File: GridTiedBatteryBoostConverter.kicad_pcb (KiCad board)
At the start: 2 copper layers, 270.1 x 143.1 mm, 160 parts, among them J101 Battery Connection, J103 Solar Panels, J202 Conn_01x03_Female, J203 I2C_BUS, J401 Screw_Terminal_01x02, J402 AudioJack2_SwitchT, Q101 IXFP36N20X3, Q102 BC847B-13-F, Q103 SSM3K329R, Q104 SSM3J334R, Q201 SSM3K329R, Q202 SSM3K329R, Q203 SSM3J334R, Q301 BC847B-13-F, Q302 BC856B-13-F, Q305 TK32A12N1,S4X, Q306 TK32A12N1,S4X, SW201 SW_Up, SW202 SW_Down, SW203 SW_Enter, U101 OPA2837DGK, U102 UCC2800DTR, U201 LCD 2004A, U202 Teensy-LC, U203 PCF8574ADWR, U204 ESP-WROOM-02U, U301 FDA217, U302 LTC7138EMSE-PBF, U303 TPS560200, U304 TLV70430_SOT23-5, U305 REF2925AIDBZT, U306 TPS560200

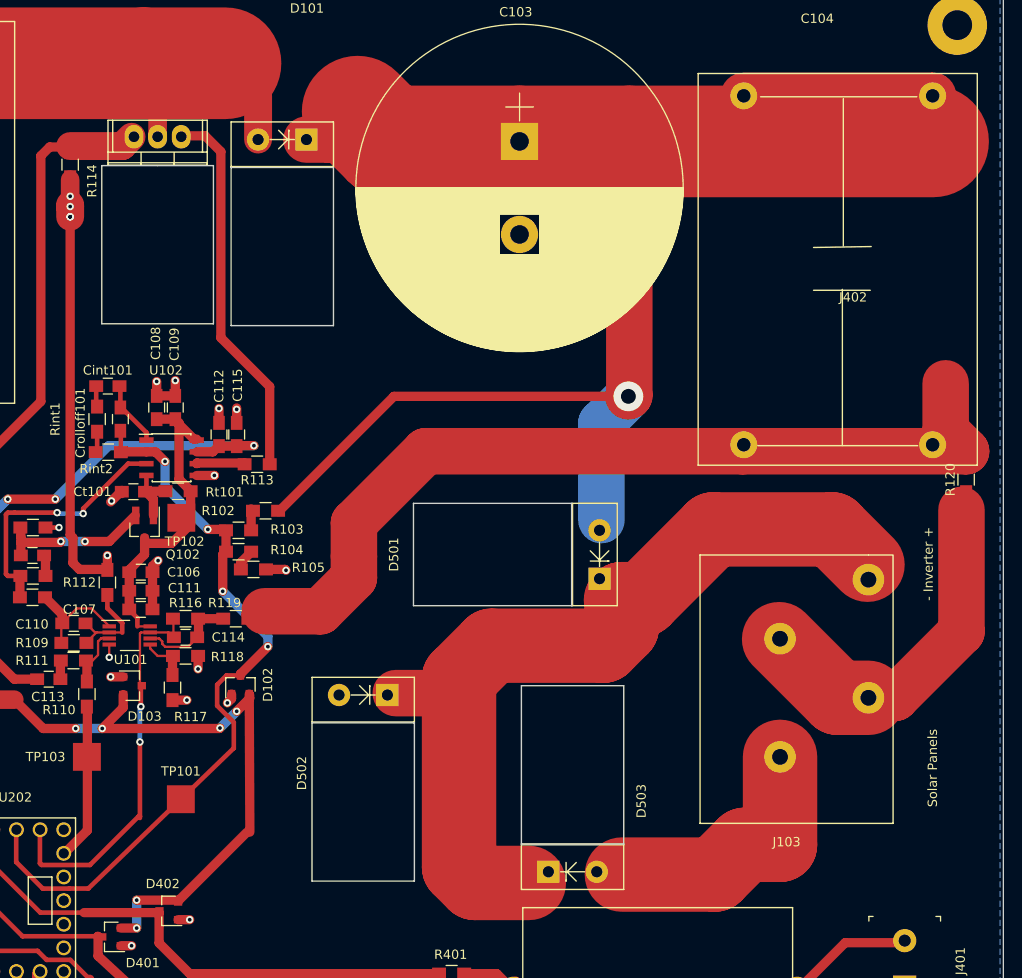
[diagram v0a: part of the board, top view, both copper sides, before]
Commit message: Consolidated a lot of part values that were the same part but not detected the same by Boms_away BOM editor because of subtle differences in how I specified the values. Added Digi-key part numbers to the resistors. Replaced 2mOhm .5W current sense resistors with 1W 2mOhm Thin Film resistors (lower inductance than metal element), And fixed a bug where I was earthing the return feed of the Solar inverter before passing through the current sense resistor.
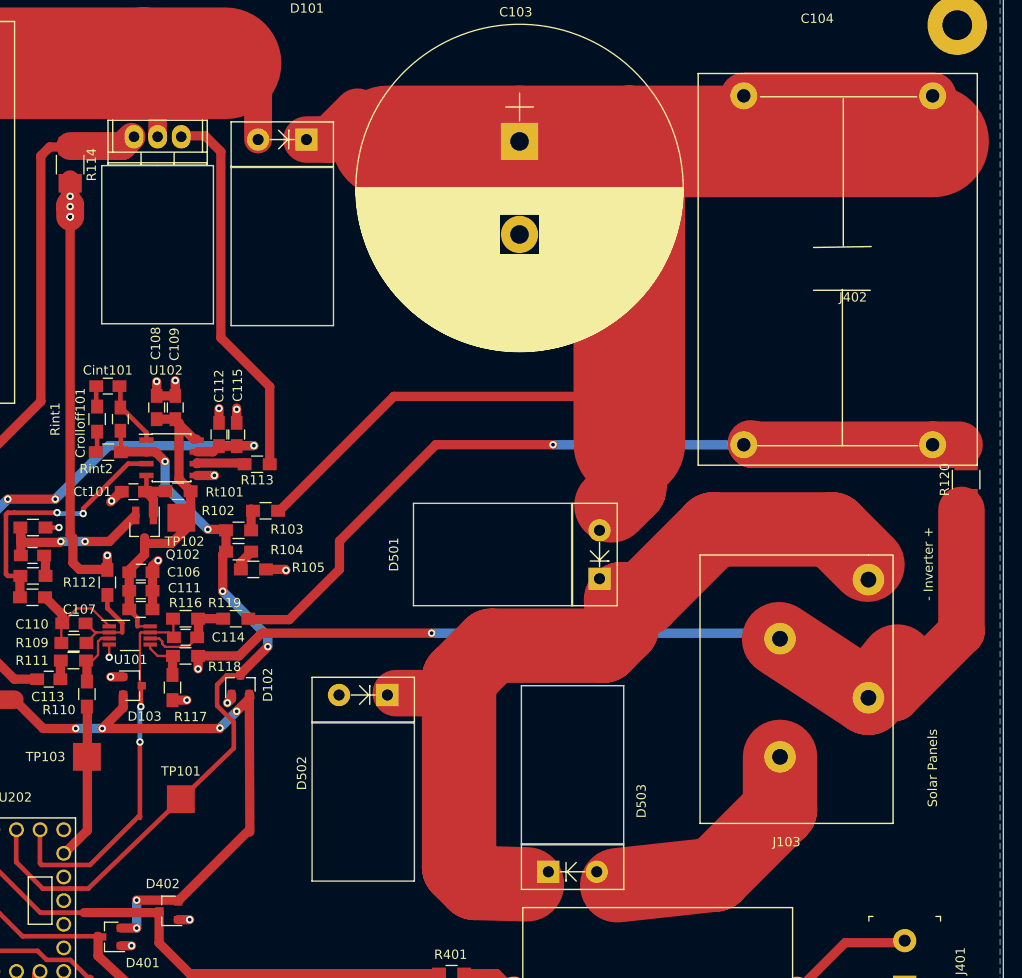
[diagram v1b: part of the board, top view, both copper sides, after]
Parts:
- C104: value 70uF 500V 2.1mOhm PP film -> 70uF PP Film 500V 2.1mOhm
- C105: value 100 pF -> 100pF
- C106, C111, C115: value 1uF 25V X7R -> 1uF X7R 25V 10%
- C107, C112: value 0.1uF mlcc -> 0.1uF X7R 25V 10%
- C108: value 1uF 16V X7R -> 1uF X7R 25V 10%
- C109: value C 0.1uF mlcc -> 0.1uF X7R 25V 10%
- C110: value 6 pF -> 6pF
- C113: value 1 nF -> 1nF
- C114: value 1 uF -> 1uF X7R 25V 10%
- C201: value 1uF x7r 16V -> 1uF X7R 25V 10%
- C202, C203, C205: value 0.1uF x7r 16V -> 0.1uF X7R 25V 10%
- C204, C301, C308: value 10uF 16V X7R -> 10uF X7R 16V
- C302: value 0.47uF x7r 25V 10% -> 0.47uF X7R 25V 10%
- C303: value 1uF 250V x7r -> 1uF X7R 250V
- C304, C309: value 0.1uF 16V X7R -> 0.1uF X7R 25V 10%
- C312: value 0.1 uF 16V X7R -> 0.1uF X7R 25V 10%
- C313: value 1 uF 25V X7R -> 1uF X7R 25V 10%
- C314: value 1uF 250V X7R -> 1uF X7R 250V
- Crolloff101: value 68 pF 5% C0G mlcc -> 68pF C0G 5%
- Ct101: value 200pF 2% C0G mlcc -> 200pF C0G 2%
- L101: value 47uH 31A Sat 6.38m Ohm -> 47uH 31A Sat 6.38m Ohm
- R102: value 82k 0.1% .25W -> 82K 0.1%
- R103: value 75k 0.1% 0.25W -> 75K 0.1%
- R104: value 1.5k 0.1% 0.25W -> 1.5K 0.1%
- R105: value 1k 0.1% 0.25W -> 1K 0.1%
- R106, R108: value 1k 1% -> 1K 1%
- R110: value 10 k 0.1% -> 10K 0.1%
- R111: value 330 Ohm .1% -> 330 0.1%
- R112: value 330 Ohm 0.1% -> 330 0.1%
- R113: value 10 ohm -> 10 1%
- R114: value 2 mOhm 0.5W -> 2 mOhm Thick Film 1% 1W; footprint Resistors_SMD:R_0805_HandSoldering -> Resistors_SMD:R_1210_HandSoldering
- R115: value 1M Ohm 1% -> 1M 1%
- R116, R117: value 10k 0.1% -> 10K 0.1%
- R118, R119: value 330 Ohms 0.1% -> 330 0.1%
- R120: value 2 mOhm 0.1% -> 2 mOhm Thick Film 1% 1W; footprint Resistors_SMD:R_0805_HandSoldering -> Resistors_SMD:R_1210_HandSoldering
- R201, R202, R203, R204: value 1K -> 1K 1%
- R205: value 100K Ohm -> 100K 1%
- R206: value 100 Ohm 1% -> 100 1%
- R208, R211, R212: value 4k7 1% -> 4K7 1%
- R303: value 61.9k 0.1% -> 61.9K 0.1%
- R304, R311: value 20k 0.1% -> 20K 0.1%
- R309: value 196k 0.1% -> 196K 0.1%
- R401: value 5.9K ohms .1% -> 5.9K 0 .1%
- R402: value 1K ohms .1% -> 1K 0.1%
- R404: value 41.2 Ohms 0.1% -> 41.2 0.1%
- R405, R406: value 10K ohms 0.1% -> 10K 0.1%
- Rint1: value 1.0k Ohm .1% -> 1K 0.1%
- Rint2: value 1.5 k Ohm -> 1.5K 0.1%
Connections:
- C104 pad 2: Net-(C104-Pad3) -> 0
- C104 pad 3: Net-(C104-Pad3) -> 0
- J103 pad 2: 0 -> Net-(J103-Pad2)
- J103 pad 3: 0 -> Net-(J103-Pad2)
- R118 pad 2: 0 -> Net-(J103-Pad2)
- R119 pad 2: Net-(C104-Pad3) -> 0
- R120 pad 1: 0 -> Net-(J103-Pad2)
- R120 pad 2: Net-(C104-Pad3) -> 0
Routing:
- net Net-(J103-Pad2): track 0.00 -> 107.7 mm, vias 0 -> 2
- net Net-(C104-Pad3): track 94.2 -> 0.00 mm
- net 0: track 260.2 -> 306.0 mm
- net Vboost_out: track 175.7 -> 169.1 mm, vias 1 -> 0
- net /Vsolar_in: track 27.8 -> 26.1 mm

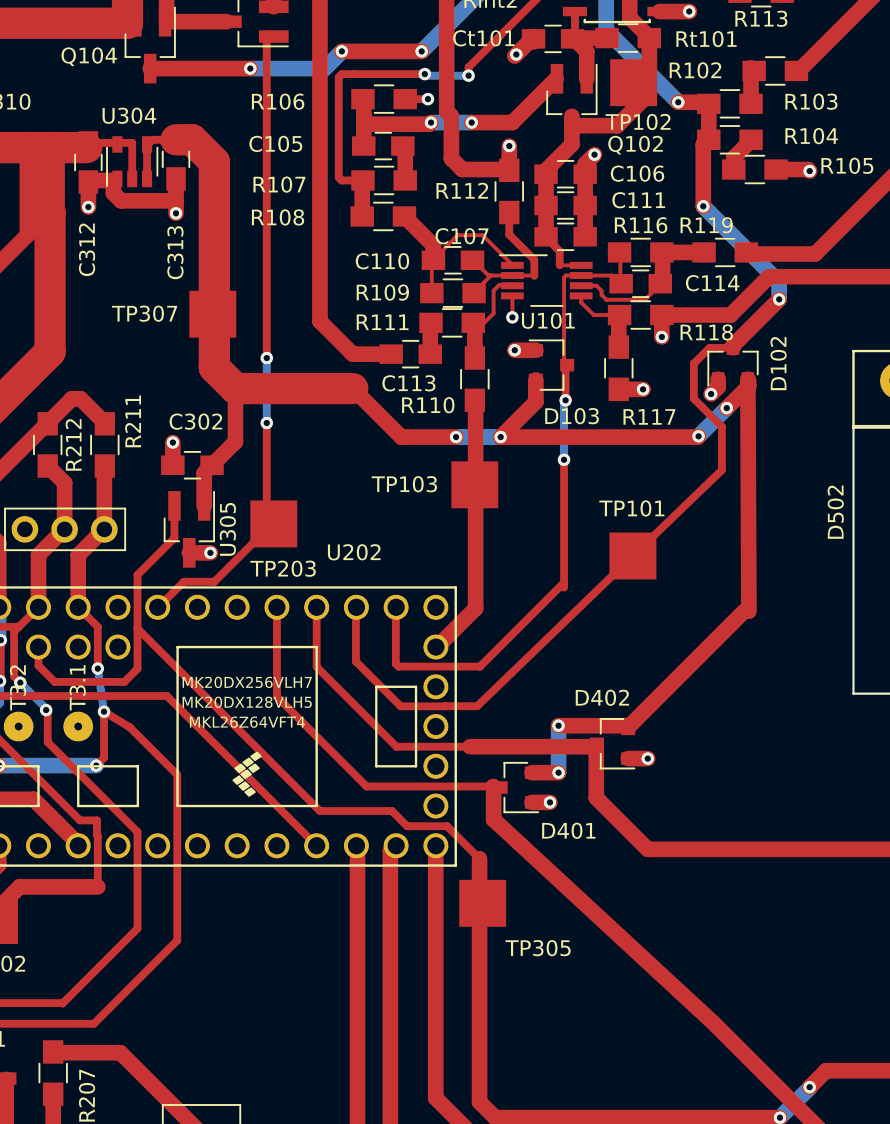
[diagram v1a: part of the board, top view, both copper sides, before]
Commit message: change a few compoents foot prints for SOT23 to SOT23-Handsoldered, and SOT23-5 to SOT23-5-Handsoldered
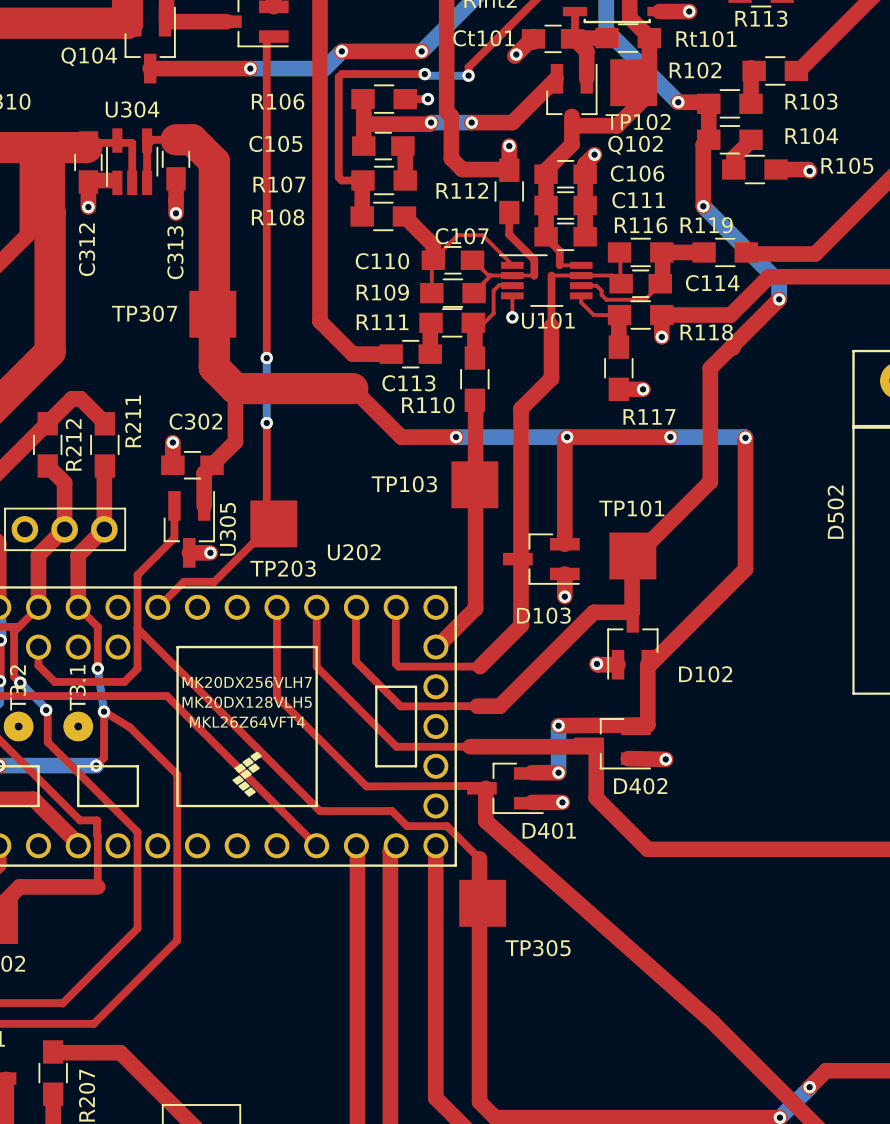
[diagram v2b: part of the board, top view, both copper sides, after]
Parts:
- D102, D103, D401, D402: footprint Package_TO_SOT_SMD:SOT-23 -> Package_TO_SOT_SMD:SOT-23_Handsoldering
- R101: value 0 Ohms -> 0R Ohms
- R111, R112, R118, R119: value 330 0.1% -> 330R 0.1%
- R113: value 10 1% -> 10R 1%
- R206: value 100 1% -> 100R 1%
- R302: value 330 1% -> 330R 1%
- U304: footprint Package_TO_SOT_SMD:SOT-23-5 -> Package_TO_SOT_SMD:SOT-23-5_HandSoldering
- moved D102 18.9 mm to (194.7, 108.2)
- moved D103 12.4 mm to (188.8, 102.9), turned to 180 degrees
- moved D401 0.70 mm to (186.6, 117.5)
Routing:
- net 0: track 306.0 -> 303.3 mm
- net +3.0V: track 105.3 -> 102.8 mm
- net Mains_Current: track 130.4 -> 128.8 mm
- net Avg_Current: track 42.6 -> 42.7 mm, vias 2 -> 0

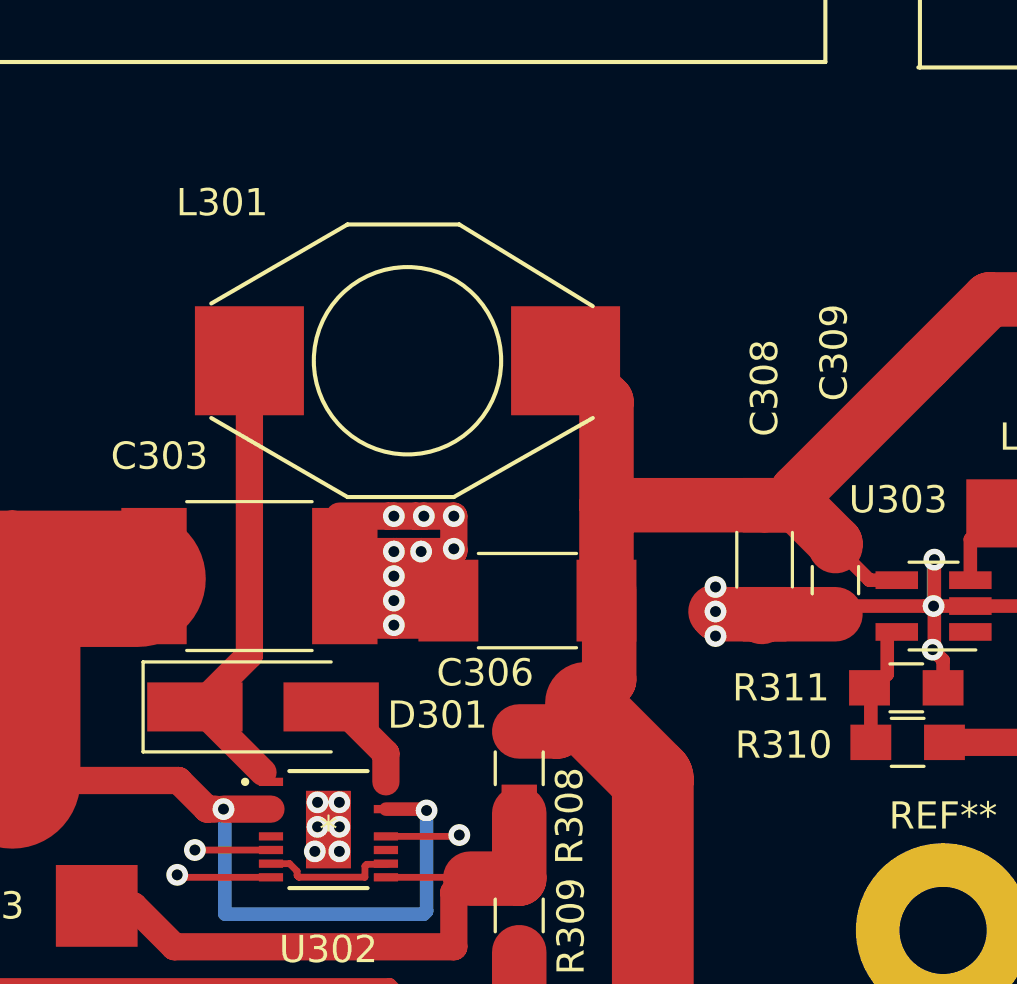
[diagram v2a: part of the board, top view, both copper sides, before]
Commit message: Finished adding digi key part numbers, for now git add *
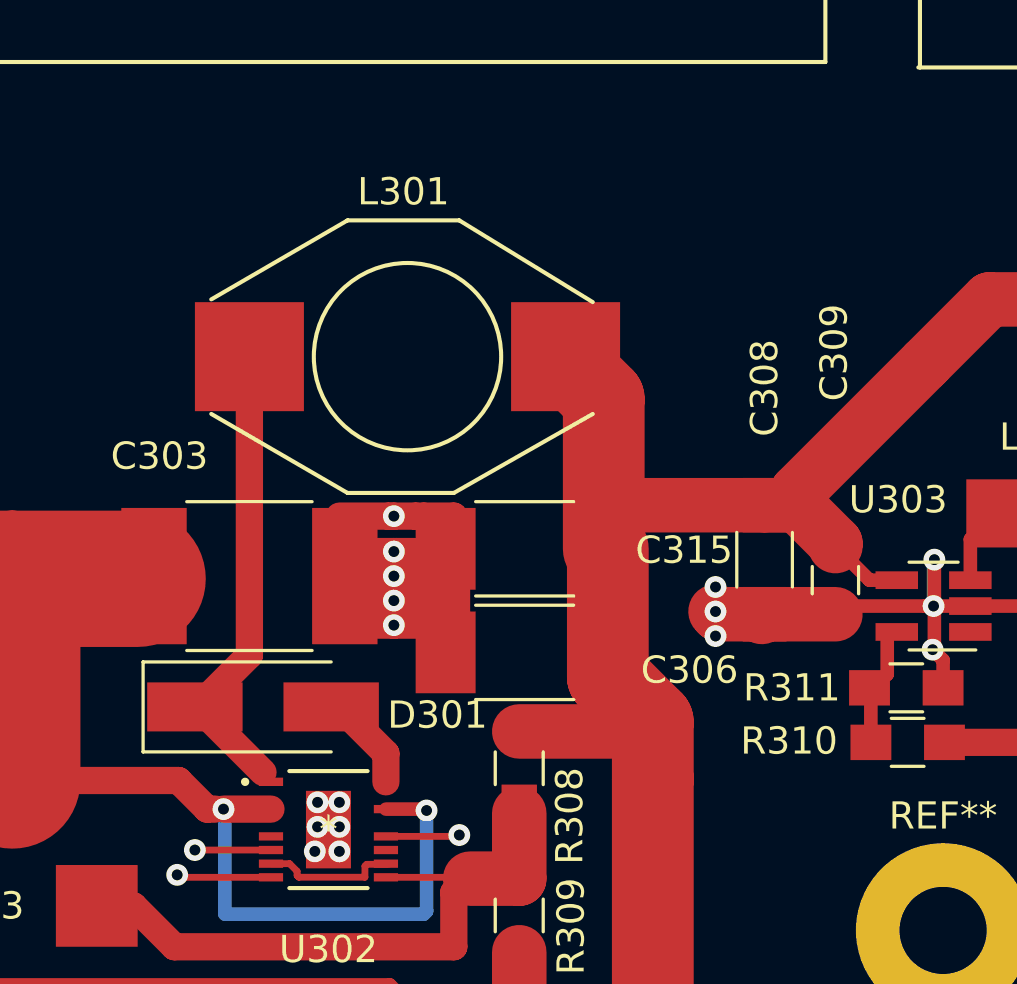
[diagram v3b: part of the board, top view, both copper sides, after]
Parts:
- added C315: 33uF X7R 16V, Capacitors_SMD:C_1812_HandSoldering, F.Cu at (126.4, 77.8)
- C110: value 6pF -> 6pF C0G
- C401: value C_Small -> 1uF X7R 25V 10%
- Cint101: value 0.56uF 10% 16V mlcc -> 0.56uF X7R 16V 10%
- moved C306 1.90 mm to (126.4, 81.6)
- moved L301 0.15 mm to (127.9, 70.8)
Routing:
- net +11V: track 177.4 -> 178.7 mm
- net 0: vias 90 -> 86

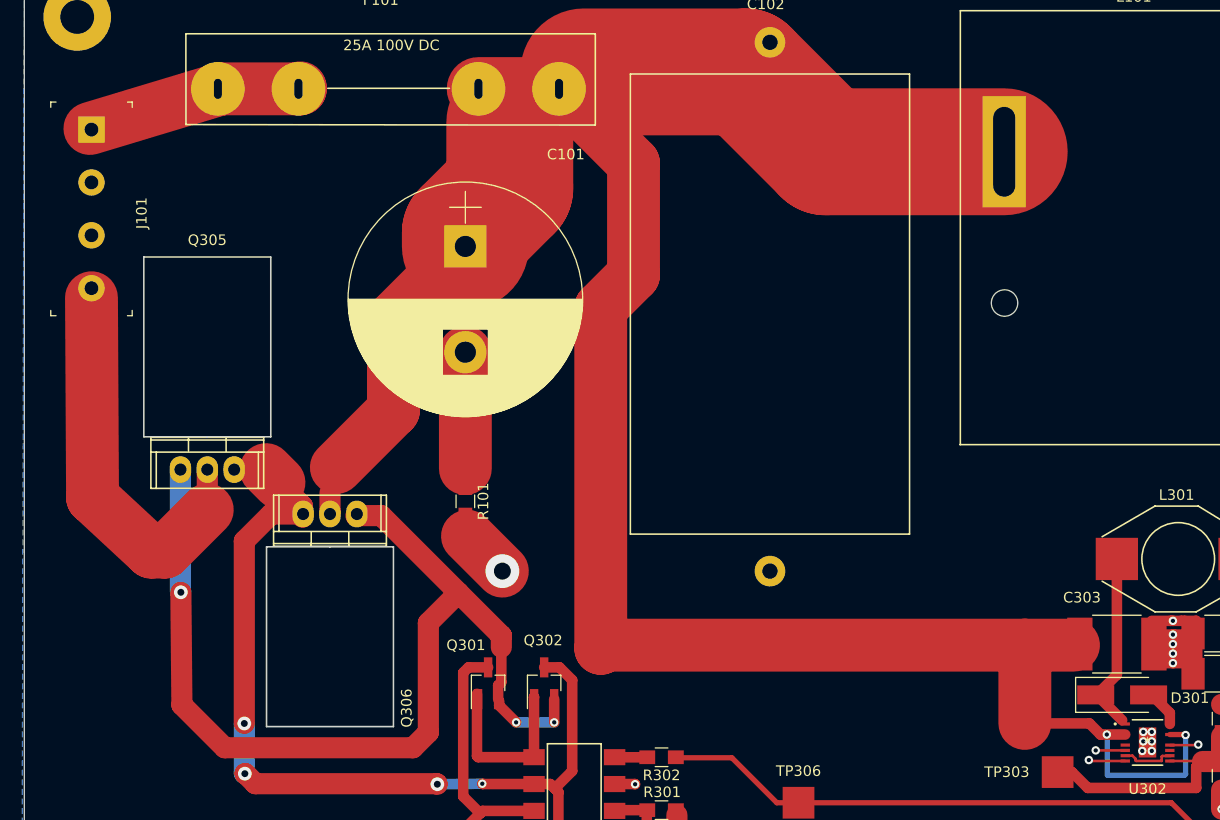
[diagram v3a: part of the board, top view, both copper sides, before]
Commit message: added thermal via of .3 drill size and .6, I have read the recomenned size is .25 drill but the smallest JLCPCB do for double sided boards is .3
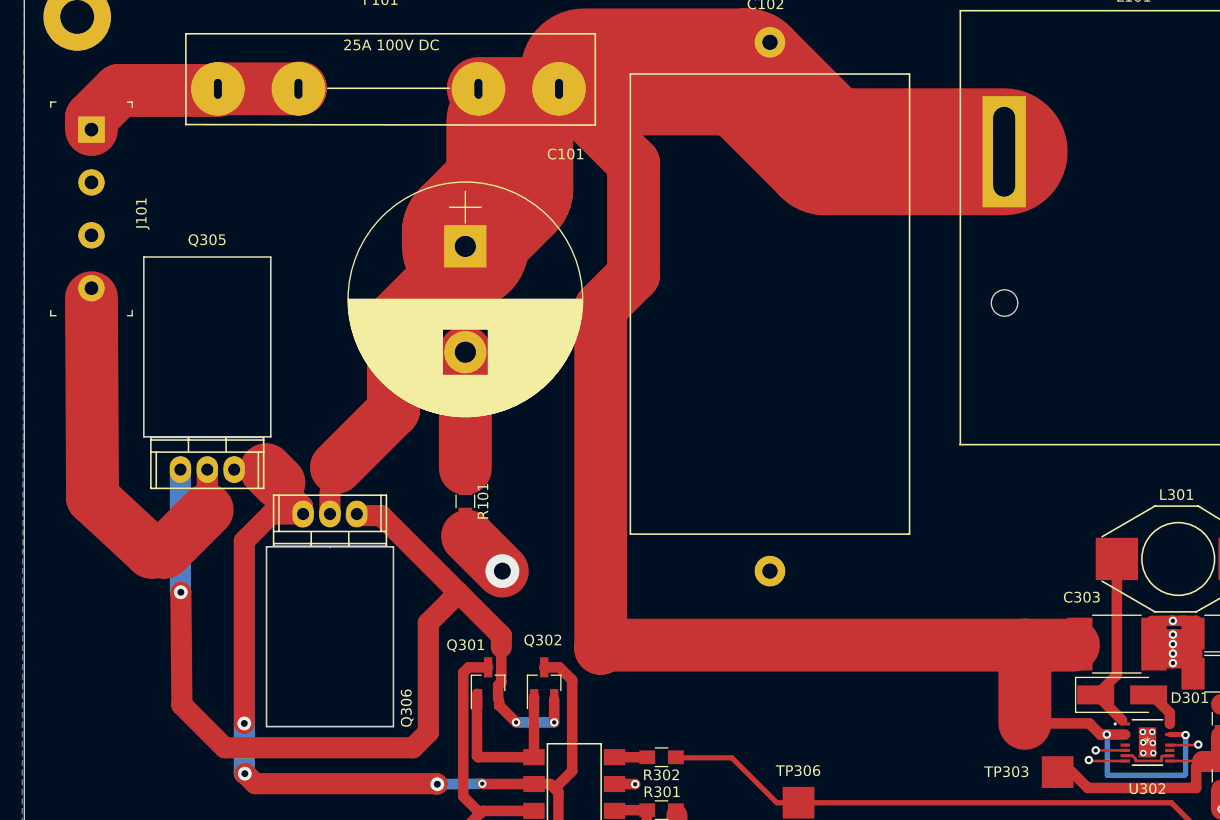
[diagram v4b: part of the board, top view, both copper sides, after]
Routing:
- net Net-(F101-Pad1): track 20.6 -> 22.2 mm
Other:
- net class u302 added: clearance 0.19, trace_width 0.25, via_dia 0.8, via_drill 0.4
